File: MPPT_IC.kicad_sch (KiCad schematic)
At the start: 0 parts

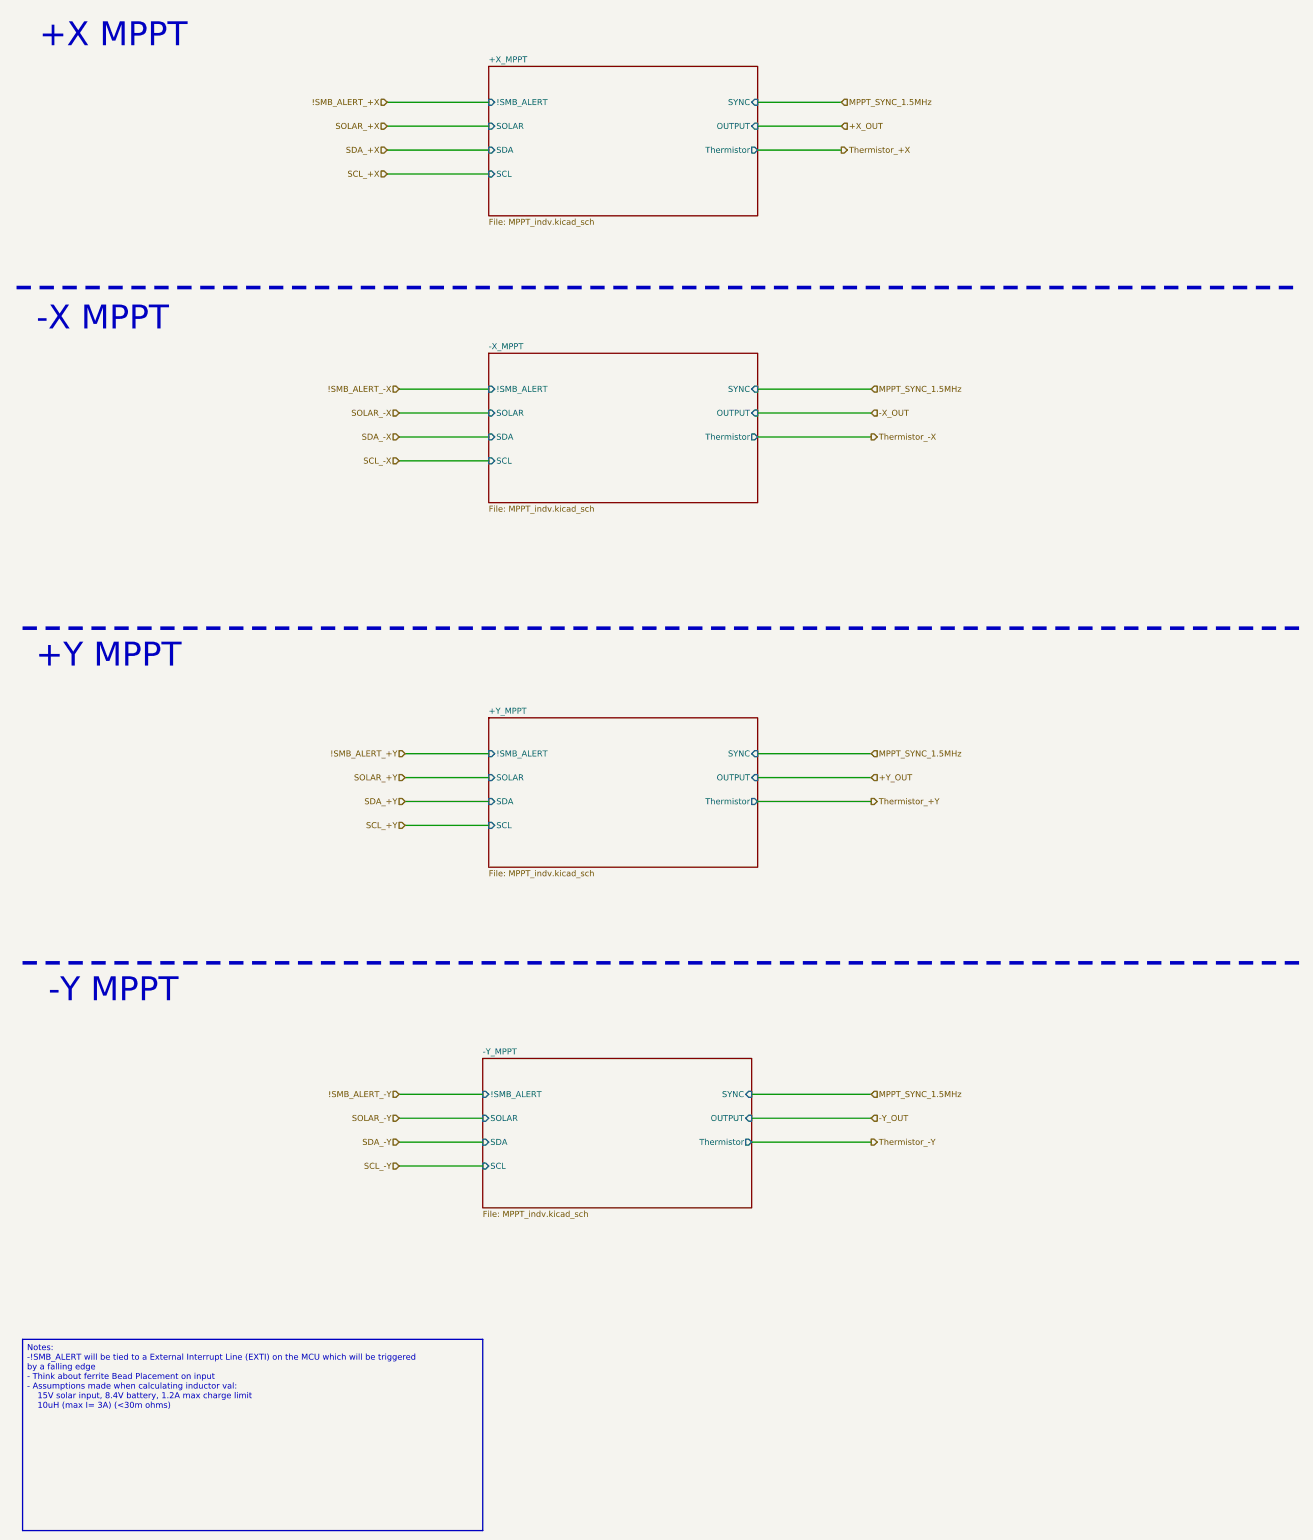
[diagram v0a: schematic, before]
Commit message: Started layout of the Ideal diode input (LTC4417)
I'm considering getting rid of the second 3V3 buck but will need to weigh the pros and cons a little more before commiting
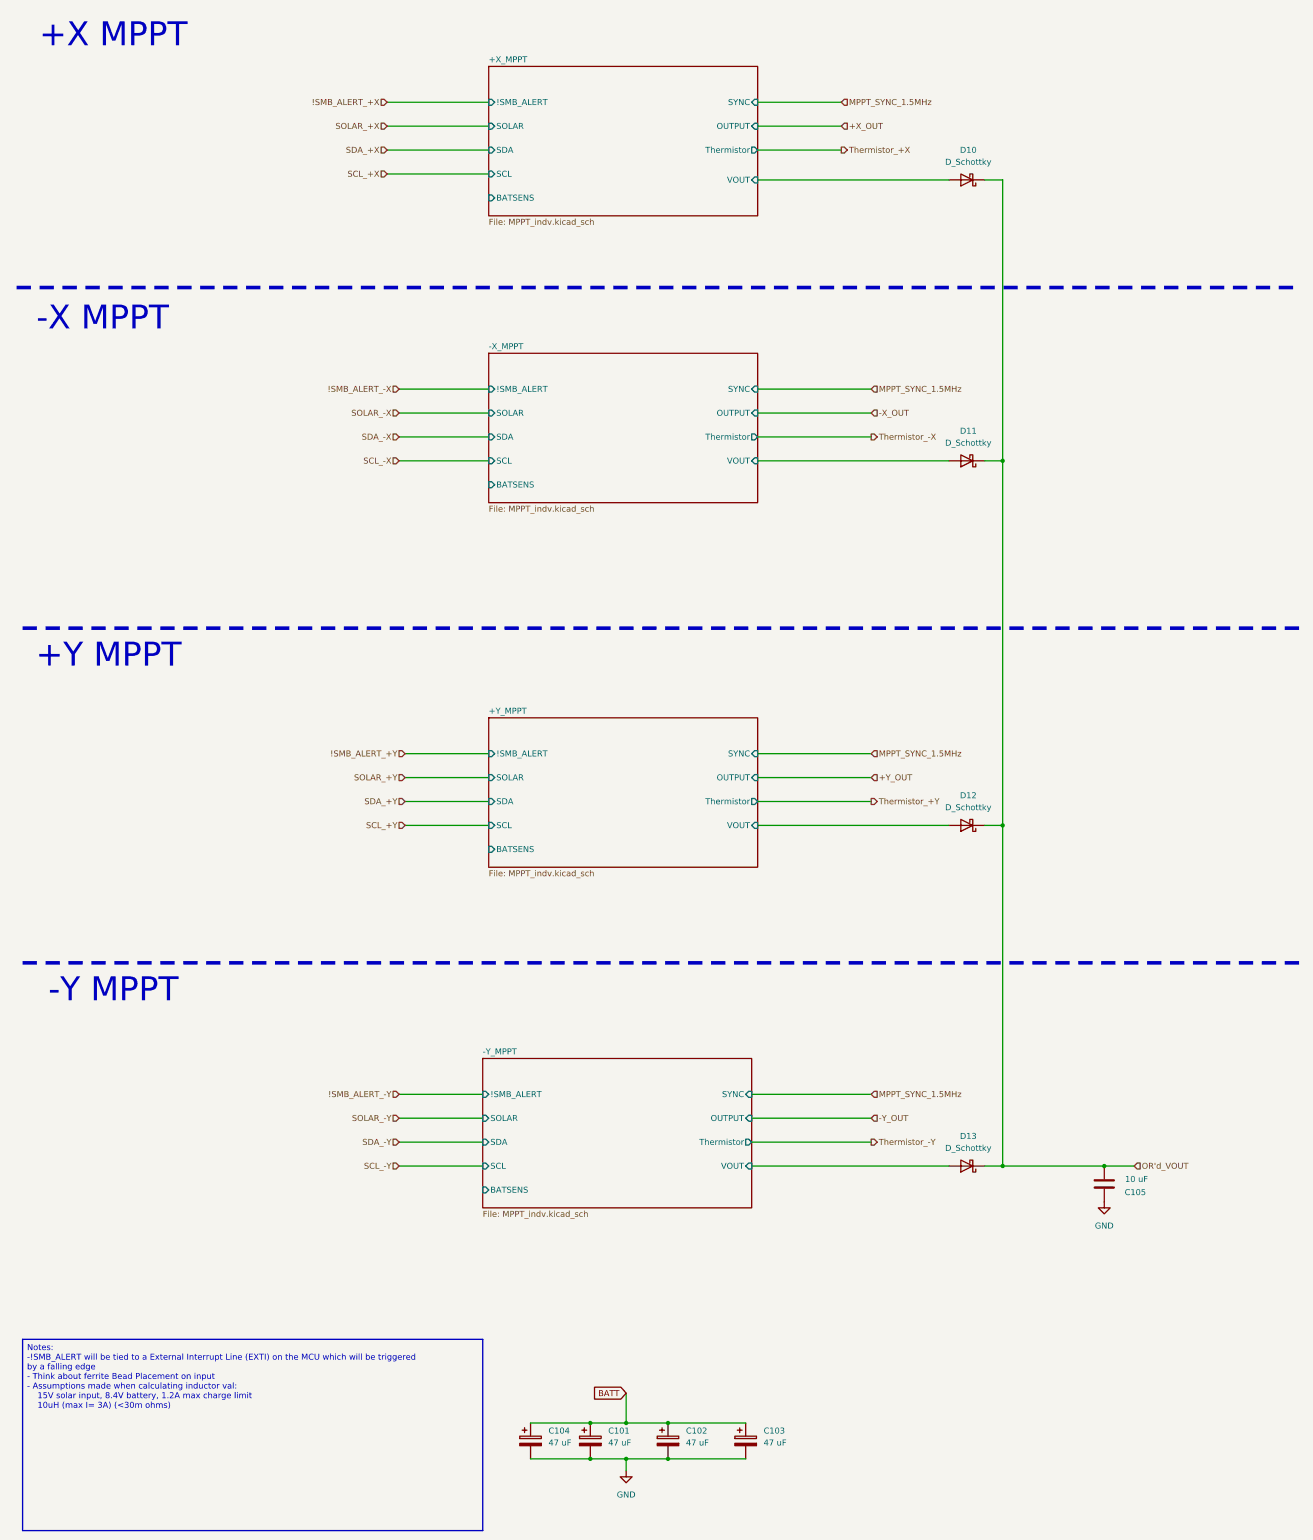
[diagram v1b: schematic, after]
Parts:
- added C101, C102, C103, C104: 47 uF, Capacitor_Tantalum_SMD:CP_EIA-7343-43_Kemet-X, symbol Device:C_Polarized
- added C105: 10 uF, Capacitor_SMD:C_1206_3216Metric, symbol Device:C
- added D10, D11, D12, D13: D_Schottky, Diode_SMD:D_SOD-128, symbol Device:D_Schottky
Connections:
- new net +X_MPPT/VOUT: D10.2 (A)
- new net +Y_MPPT/VOUT: D12.2 (A)
- new net -X_MPPT/VOUT: D11.2 (A)
- new net -Y_MPPT/VOUT: D13.2 (A)
- new net BATT: C101.1, C102.1, C103.1, C104.1
- new net GND: C101.2, C102.2, C103.2, C104.2, C105.1
- new net OR'd_VOUT: C105.2, D10.1 (K), D11.1 (K), D12.1 (K), D13.1 (K)
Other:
- sheet +X_MPPT ports: added BATSENS, VOUT; removed none
- sheet +Y_MPPT ports: added BATSENS, VOUT; removed none
- sheet -X_MPPT ports: added BATSENS, VOUT; removed none
- sheet -Y_MPPT ports: added BATSENS, VOUT; removed none

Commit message: Efuses for this board and Battery board
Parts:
- renumbered C104 to C17, C101 to C18, C102 to C19, C103 to C20, C105 to C21, D10 to D3, D11 to D4, D12 to D5, D13 to D6
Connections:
- net BATT renamed BATT_1
- net BATT_1: no longer C17.1, C19.1
- new net BATT_2: C17.1, C19.1
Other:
- moved on the sheet: C18, C19
